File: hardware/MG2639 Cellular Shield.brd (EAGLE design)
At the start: 53.3 x 73.7 mm, 48 parts, among them J1 SIMHOLDER, Q1 MMBT2222A, U1 TXB0108, U2 SPX29302, U4 ARDUINO_R3_SHIELD, U5 MG2639V3

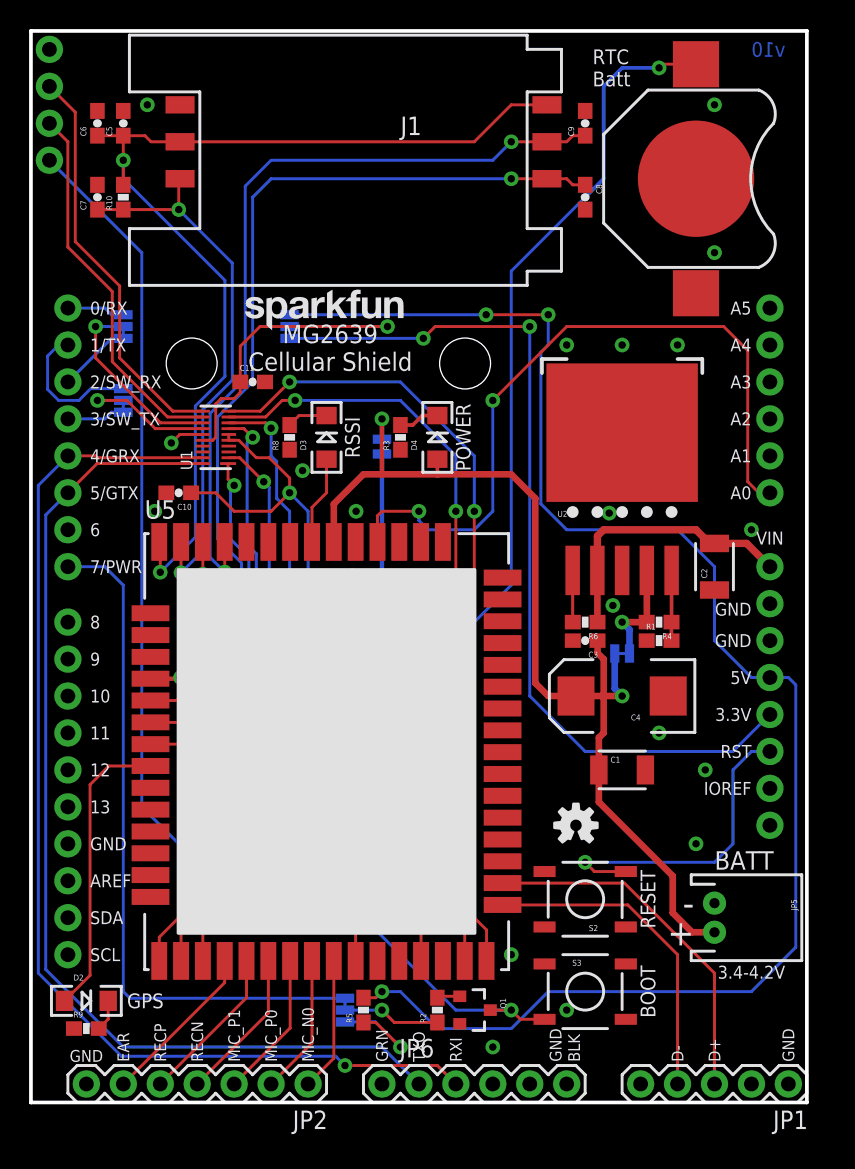
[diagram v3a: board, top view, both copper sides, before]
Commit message: re-routing around TXB0108, cleaning up some silk.
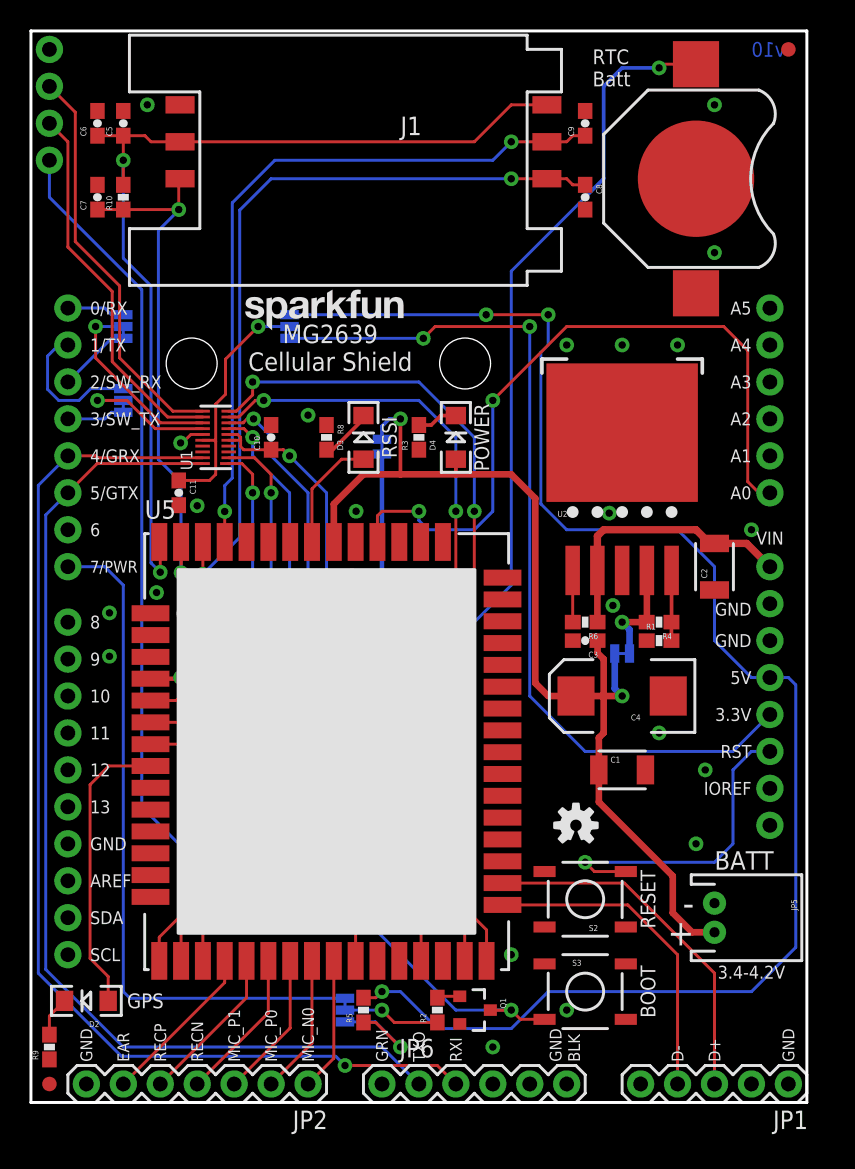
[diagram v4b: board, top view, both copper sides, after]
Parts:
- added FID1, FID2: FIDUCIAL1X2, SparkFun-Aesthetics:FIDUCIAL-1X2
- moved C11 9.16 mm to (10.2, 41.9), turned to 270 degrees
- moved C10 7.41 mm to (16.5, 45.7), turned to 90 degrees
- moved R9 2.84 mm to (1.27, 3.81), turned to 90 degrees
- moved D3 2.54 mm to (22.9, 45.7)
- moved R8 2.54 mm to (20.3, 45.7), turned to 270 degrees
- moved R3 1.27 mm to (26.7, 45.7)
- moved D4 1.27 mm to (29.2, 45.7)
- turned D2 to 180 degrees
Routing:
- net VCCB: track 25.9 -> 17.2 mm
- net SIM_RST: track 54.8 -> 49.7 mm
- net VDDIO: track 53.4 -> 48.5 mm
- net SIM_CLK: track 56.9 -> 53.1 mm
- net VSIM: track 70.7 -> 68.3 mm
- net N$7: track 6.10 -> 8.03 mm
- net SIM_DATA: track 37.9 -> 36.1 mm
- net RX-2.8V: track 41.1 -> 42.6 mm
- net TX2-2.8V: track 54.9 -> 56.1 mm
- net 3.8V: track 71.0 -> 71.9 mm
- net TX-2.8V: track 43.3 -> 44.2 mm
- net N$8: track 2.81 -> 3.65 mm
- net RX2-2.8V: track 52.6 -> 53.4 mm
- net GND: track 2.39 -> 1.75 mm, vias 22 -> 26
- net N$9: track 2.17 -> 2.76 mm
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
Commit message: adding 22 ohm resistors to D+/D-. placing more vias around vreg.
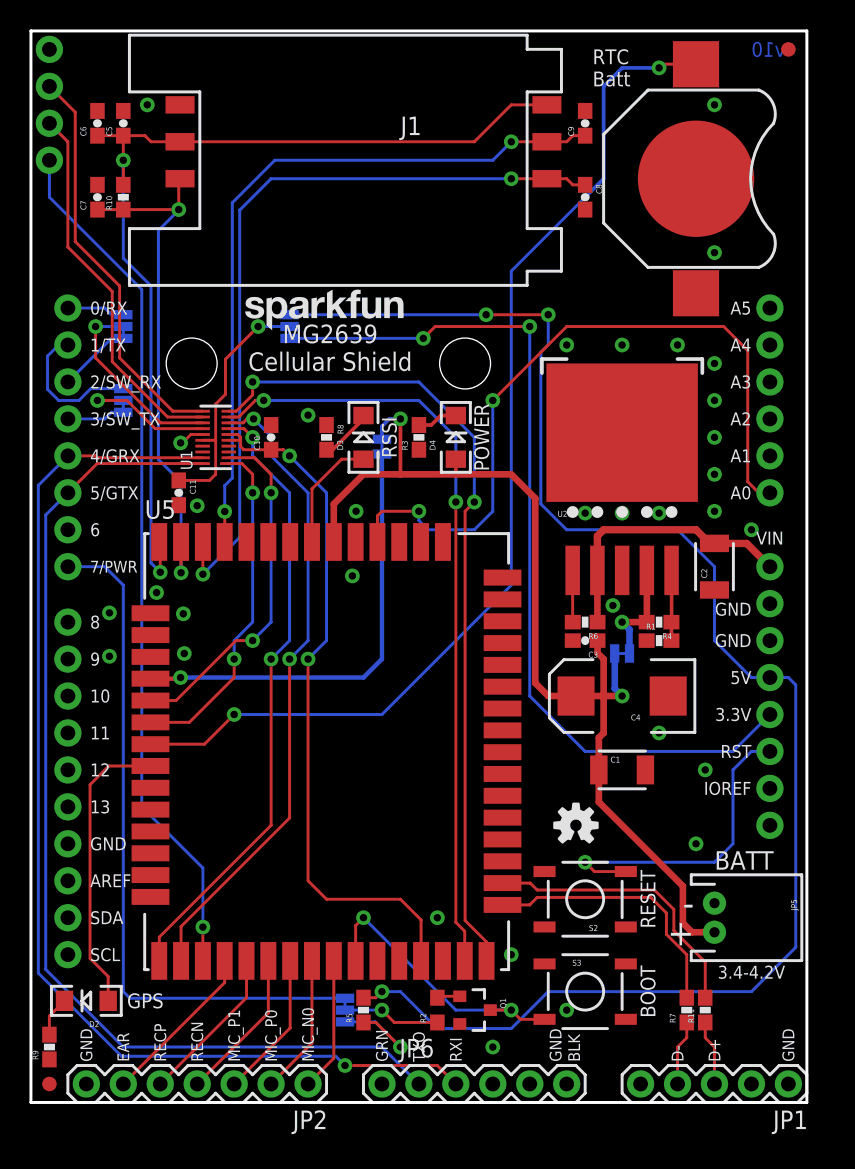
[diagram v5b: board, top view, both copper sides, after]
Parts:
- added R11, R7: 22, SparkFun-Resistors:0603-RES
- R2: device SparkFun-Resistors:0603-RES -> SparkFun-Resistors:0603
- moved FRAME1 28.1 mm to (-7.62, -22.9)
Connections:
- new net N$10: JP1.3, R11.1
- new net N$2: JP1.4, R7.1
- net USB+: now also R11.2; no longer JP1.3
- net USB-: now also R7.2; no longer JP1.4
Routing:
- net USB+: track 24.8 -> 19.5 mm
- net N$10: track 0.00 -> 4.49 mm
- net N$2: track 0.00 -> 4.49 mm
- net USB-: track 22.3 -> 18.3 mm
- net TX2-2.8V: track 56.1 -> 56.7 mm
- net GND: vias 26 -> 33

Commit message: rearranging LEDs - moving GPS LED up with others.
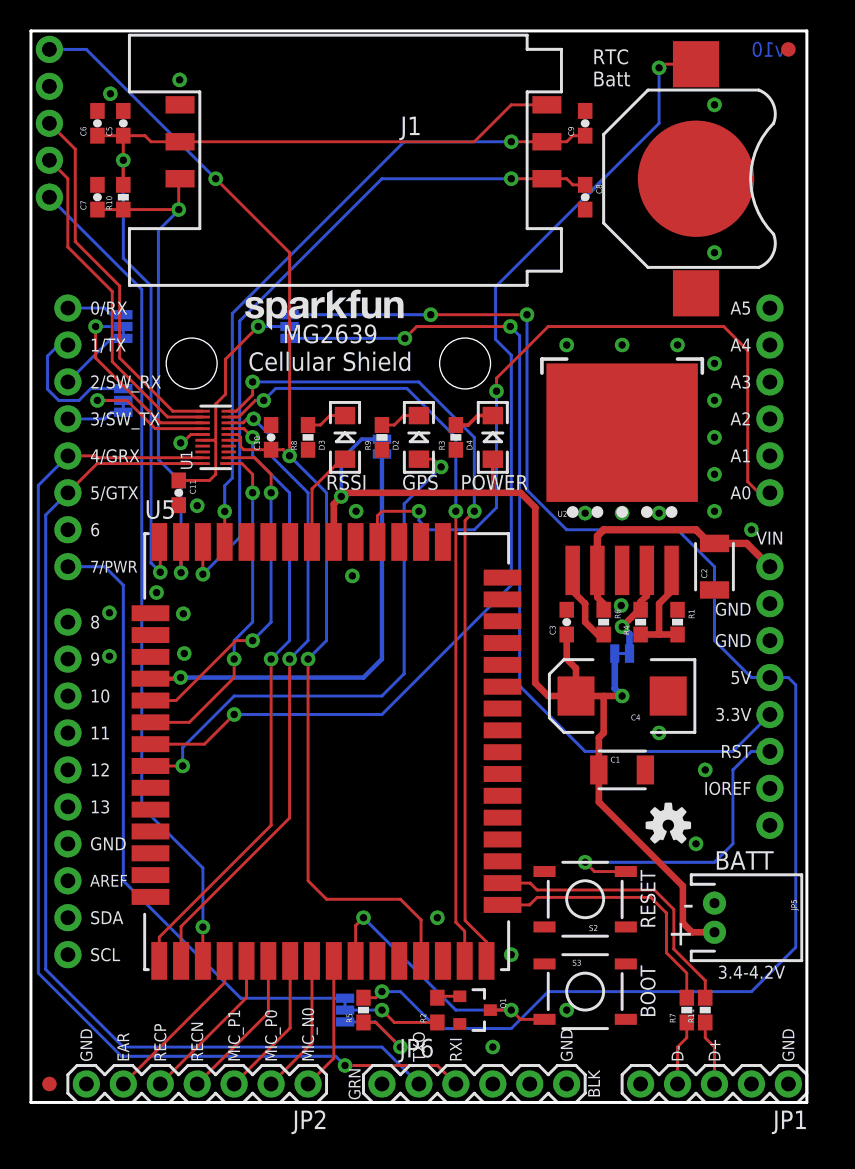
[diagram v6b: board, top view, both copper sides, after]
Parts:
- added JP7: M01PTH, SparkFun-Connectors:1X01
- moved R9 47.7 mm to (24.1, 45.7)
- moved D2 45.0 mm to (26.7, 45.7), turned to 90 degrees
- moved LOGO2 6.35 mm to (43.8, 19.1)
- moved JP4 2.54 mm to (1.27, 64.8)
- moved D4 2.54 mm to (31.8, 45.7)
- moved JP3 2.54 mm to (1.27, 62.2)
- moved R3 2.54 mm to (29.2, 45.7)
- moved C3 1.80 mm to (36.8, 33.0), turned to 90 degrees
- moved R1 1.80 mm to (44.5, 33.0), turned to 270 degrees
- moved R4 1.27 mm to (41.9, 33.0), turned to 90 degrees
- moved D3 1.27 mm to (21.6, 45.7)
- moved R8 1.27 mm to (19.1, 45.7), turned to 90 degrees
- moved R6 1.27 mm to (39.4, 33.0), turned to 270 degrees
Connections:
- new net ADCIN: U5.28
- new net GPIO0: U5.55
- new net GPIO1: U5.54
- new net GPIO2: U5.53
- net VDDIO: now also JP7.1
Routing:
- net VDDIO: track 48.5 -> 84.7 mm, vias 2 -> 3
- net GPS_FIX: track 20.1 -> 37.8 mm, vias 0 -> 2
- net ON/OFF: track 47.7 -> 43.2 mm
- net SIM_RST: track 49.7 -> 45.2 mm
- net SIM_CLK: track 53.1 -> 48.6 mm
- net RX2-HV: track 26.0 -> 23.4 mm
- net !SYSRST: track 59.4 -> 56.9 mm
- net TX2-HV: track 27.9 -> 25.3 mm
- net ADJUST: track 4.83 -> 7.30 mm
- net N$1: track 3.56 -> 5.53 mm
- net 5V: track 107.9 -> 106.7 mm
- net N$7: track 8.03 -> 6.76 mm
- net N$4: track 7.62 -> 6.69 mm
- net N$8: track 3.65 -> 2.81 mm
- net 3.3V: track 61.4 -> 60.6 mm
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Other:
- board text added: "2.8V"

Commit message: Switching TXB0108 to a TXB0104. Breaking out I2C pins, 2.8V. Fixing some silk.
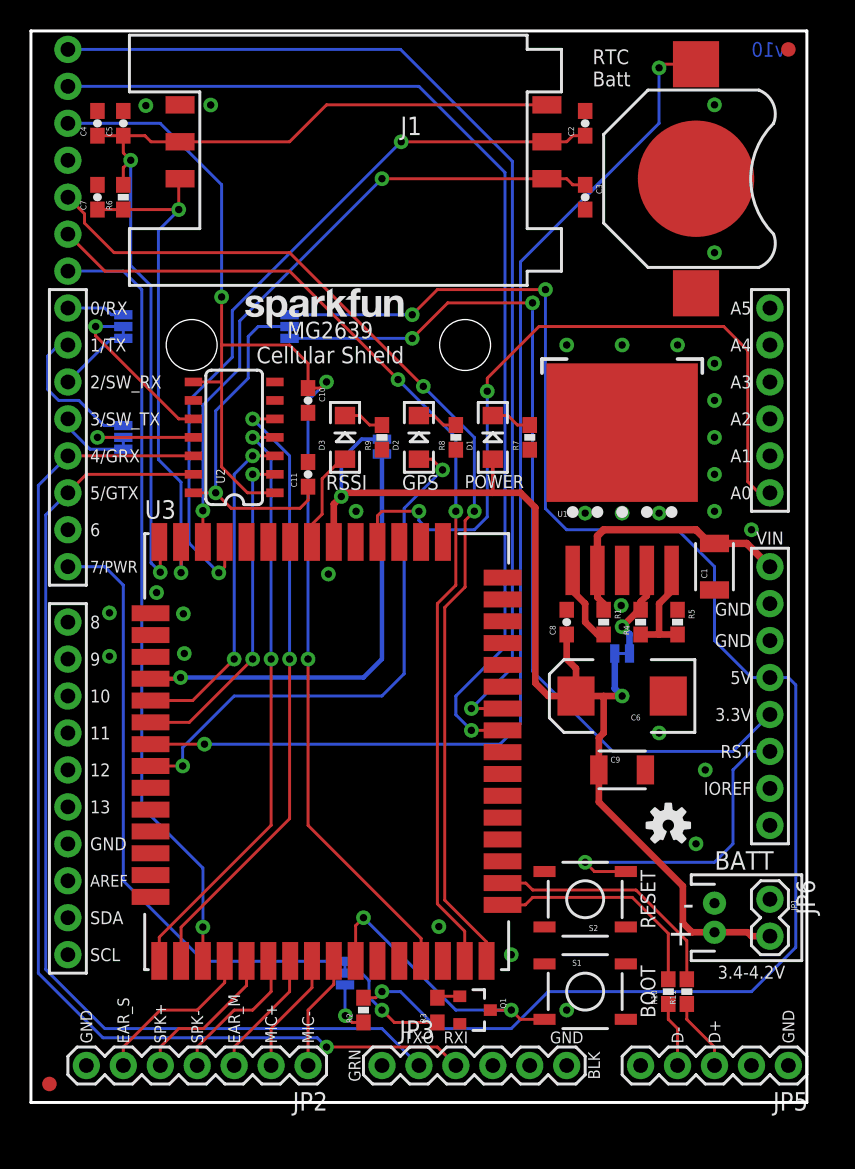
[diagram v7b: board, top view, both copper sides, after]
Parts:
- removed JP7: M01PTH, SparkFun-Connectors:1X01
- removed LOGO4: SFE_LOGO_NAME.1_INCH, SparkFun-Aesthetics:SFE_LOGO_NAME_.1
- added LOGO1: SFE_LOGO_NAME.1_INCH, SparkFun-Aesthetics:SFE_LOGO_NAME_.1
- C2: value 10uF -> 33pF; device SparkFun-Capacitors:1210 -> SparkFun-Capacitors:0603-CAP
- C3: value 0.1uF -> 33pF
- C4: value 100uF -> 1.0uF; device SparkFun-Capacitors:EIA7343 -> SparkFun-Capacitors:0603-CAP
- C6: value 1.0uF -> 100uF; device SparkFun-Capacitors:0603-CAP -> SparkFun-Capacitors:EIA7343
- C8: value 33pF -> 0.1uF
- C9: value 33pF -> 10uF; device SparkFun-Capacitors:0603-CAP -> SparkFun-Capacitors:1210
- JP1: value (none) -> LiPo; device SparkFun-Connectors:1X05 -> SparkFun-Connectors:JST-2-PTH
- JP3: value M01PTH -> FTDI_BASICPTH; device SparkFun-Connectors:1X01 -> SparkFun-Connectors:FTDI_BASIC
- JP4: device SparkFun-Connectors:1X03 -> SparkFun-Connectors:1X07
- JP5: value LiPo -> (none); device SparkFun-Connectors:JST-2-PTH -> SparkFun-Connectors:1X05
- JP6: value FTDI_BASICPTH -> M02PTH; device SparkFun-Connectors:FTDI_BASIC -> SparkFun-Connectors:1X02
- LOGO2: value OSHW-LOGOS -> SFE_LOGO_NAME_FLAME.2_INCH; device SparkFun-Aesthetics:OSHW-LOGO-S -> SparkFun-Aesthetics:SFE_LOGO_NAME_FLAME_.2
- LOGO3: value SFE_LOGO_NAME_FLAME.2_INCH -> OSHW-LOGOS; device SparkFun-Aesthetics:SFE_LOGO_NAME_FLAME_.2 -> SparkFun-Aesthetics:OSHW-LOGO-S
- R1: value 1K -> 10K
- R10: value 10K -> 22
- R2: value 4.7K -> 1K; device SparkFun-Resistors:0603 -> SparkFun-Resistors:0603-RES
- R3: value 1K -> 4.7K; device SparkFun-Resistors:0603-RES -> SparkFun-Resistors:0603
- R7: value 22 -> 1K
- SJ1, SJ6: device SparkFun-Passives:PAD-JUMPER-2-NC_BY_TRACE_YES_SILK -> SparkFun-Passives:PAD-JUMPER-3-2OF3_NC_BY_TRACE_YES_SILK_FULL_BOX
- SJ2, SJ3: device SparkFun-Passives:PAD-JUMPER-3-2OF3_NC_BY_TRACE_YES_SILK_FULL_BOX -> SparkFun-Passives:PAD-JUMPER-2-NC_BY_TRACE_YES_SILK
- U1: value TXB0108 -> SPX29302; device Testing:UFDFN-20 -> SparkFun-PowerIC:Q5-DD_SPX29300
- U2: value SPX29302 -> (none); device SparkFun-PowerIC:Q5-DD_SPX29300 -> SparkFun-DigitalIC:SO14
- moved R10 66.2 mm to (43.8, 7.62)
- moved JP3 63.9 mm to (24.1, 2.54), flipped to the top, turned to 0 degrees
- moved C4 53.4 mm to (4.57, 67.3), turned to 90 degrees
- moved C6 53.4 mm to (40.6, 27.9), turned to 180 degrees
- moved C9 44.5 mm to (40.6, 22.9), turned to 0 degrees
- moved R6 44.1 mm to (6.35, 62.2), turned to 90 degrees
- moved SJ6 41.0 mm to (6.35, 53.3), turned to 270 degrees
- moved R7 40.8 mm to (34.3, 45.7)
- moved R3 39.4 mm to (27.9, 6.35)
- moved SJ1 36.3 mm to (21.6, 8.89), turned to 90 degrees
- moved R5 34.3 mm to (44.5, 33.0), turned to 270 degrees
- moved C2 31.8 mm to (38.1, 67.3)
- moved SJ2 31.0 mm to (40.6, 30.9), turned to 0 degrees
- moved JP6 29.5 mm to (50.8, 14.0), turned to 270 degrees
- moved C3 29.2 mm to (38.1, 62.2), turned to 270 degrees
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- renumbered D4 to D1, S3 to S1, U4 to J2, U5 to U3
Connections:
- removed net GPIO0: U3.55
- removed net GPIO1: U3.54
- removed net GPIO2: U3.53
- removed net HJ: U1.3
- removed net JK: U1.4
- removed net KK: U1.18
- removed net LL: U1.17
- removed net RX2-HV: JP4.1, U1.12
- removed net TX2-HV: JP4.2, U1.11
- new net GPIO1/SCL: JP4.1, U3.54
- new net GPIO2/SDA: JP4.2, U3.53
- net !SYSRST: now also JP4.7; no longer JP3.1
- net 3.3V: now also SJ4.3; no longer SJ5.3
- net 3.8V: now also C6.A, C8.1, C9.1, JP1.2, JP6.2, SJ2.2, SJ3.1; no longer C1.1, C3.1, C4.A, JP5.2, SJ1.1, SJ6.2
- net 5V: now also R2.2, SJ4.1; no longer R5.2, SJ5.1
- net ADJUST: now also R5.2, U1.5; no longer R1.2, U2.5
- net GND: now also C1.1, C2.2, C4.2, C6.C, JP3.GND, JP4.4, JP6.1, R5.1, R7.1, U1.3, U1.6, U2.7; no longer C1.2, C2.1, C4.C, C6.2, JP4.3, JP6.GND, R1.1, R3.1, U1.15, U2.3, U2.6
- net GRX-2.8V: now also U2.3; no longer U1.2
- net GRX-HV: now also JP3.TXO, U2.12; no longer JP6.TXO, U1.19
- net GTX-2.8V: now also U2.2; no longer U1.1
- net GTX-HV: now also JP3.RXI, U2.13; no longer JP6.RXI, U1.20
- net N$1: now also R1.2, U1.1; no longer R6.2, U2.1
- net N$10: now also JP5.3; no longer JP1.3
- net N$17: now also R7.2; no longer R3.2
- net N$2: now also JP5.4, R10.1; no longer JP1.4, R7.1
- net N$3: now also R3.2; no longer R2.2
- net N$4: now also SJ2.1, U1.4; no longer SJ6.1, U2.4
- net N$5: now also R3.1, SJ1.2; no longer R2.1, SJ2.2
- net N$6: now also R2.1, SJ1.1; no longer R5.1, SJ2.1
- net N$8: now also R9.2; no longer R8.2
- net N$9: now also R8.2; no longer R9.2
- net ON/OFF: now also SJ1.3; no longer SJ2.3
- net RX-2.8V: now also U2.4; no longer U1.7
- net RX-HV: now also SJ5.2, U2.11; no longer SJ3.2, U1.14
- net RX-SOFT: now also SJ6.3; no longer SJ4.3
- net RX2-2.8V: now also JP4.6; no longer U1.9
- net RXI: now also SJ6.1; no longer SJ4.1
- net SIM_CLK: now also C3.1; no longer C8.1
- net SIM_DATA: now also R6.1; no longer R10.1
- net SIM_RST: now also C2.1; no longer C9.1
- net TX-2.8V: now also U2.5; no longer U1.8
- net TX-HV: now also SJ6.2, U2.10; no longer SJ4.2, U1.13
- net TX-SOFT: now also SJ5.3; no longer SJ3.3
- net TX2-2.8V: now also JP4.5; no longer U1.10
- net TXO: now also SJ5.1; no longer SJ3.1
- net USB-: now also R10.2; no longer R7.2
- net VCCB: now also SJ4.2, U2.14; no longer SJ5.2, U1.16
- net VDDIO: now also JP4.3, U2.1, U2.8; no longer JP7.1, U1.5, U1.6
- net VRAW: now also C1.2, R1.1, U1.2; no longer C2.2, R6.1, U2.2
- net VSIM: now also C4.1, R6.2; no longer C6.1, R10.2
- net V_GPS: now also SJ3.2; no longer SJ1.2
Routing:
- net GPIO2/SDA: track 0.00 -> 74.8 mm, vias 0 -> 1
- net GPIO1/SCL: track 0.00 -> 74.7 mm, vias 0 -> 1
- net TX2-HV: track 25.3 -> 0.00 mm
- net RX2-HV: track 23.4 -> 0.00 mm
- net TX2-2.8V: track 56.7 -> 73.2 mm
- net RX2-2.8V: track 54.1 -> 69.8 mm
- net VCCB: track 17.2 -> 24.3 mm
- net VDDIO: track 84.7 -> 91.2 mm
- net SIM_RST: track 45.2 -> 51.6 mm
- net GPS_RTC: track 72.6 -> 77.7 mm
- net N$6: track 8.36 -> 3.56 mm
- net SIM_CLK: track 48.6 -> 44.2 mm
- net 3.8V: track 72.0 -> 76.0 mm
- net !SYSRST: track 56.9 -> 53.5 mm
- net 5V: track 106.7 -> 109.9 mm
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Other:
- board text added: "EAR_M"
- board text added: "EAR_S"
- board text added: "GPIO/2SDA"
- board text added: "GPIO1/SCL"
- board text added: "MIC+"
- board text added: "MIC-"
- board text added: "SPK+"
- board text added: "SPK-"
- board text removed: "EAR"
- board text removed: "MIC_N0"
- board text removed: "MIC_P0"
- board text removed: "MIC_P1"
- board text removed: "RECN"
- board text removed: "RECP"

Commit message: Routing UART1 to FTDI header instead of GPS. Adding TP's. Fixing silk. Routing out GPS battery pull-out area.
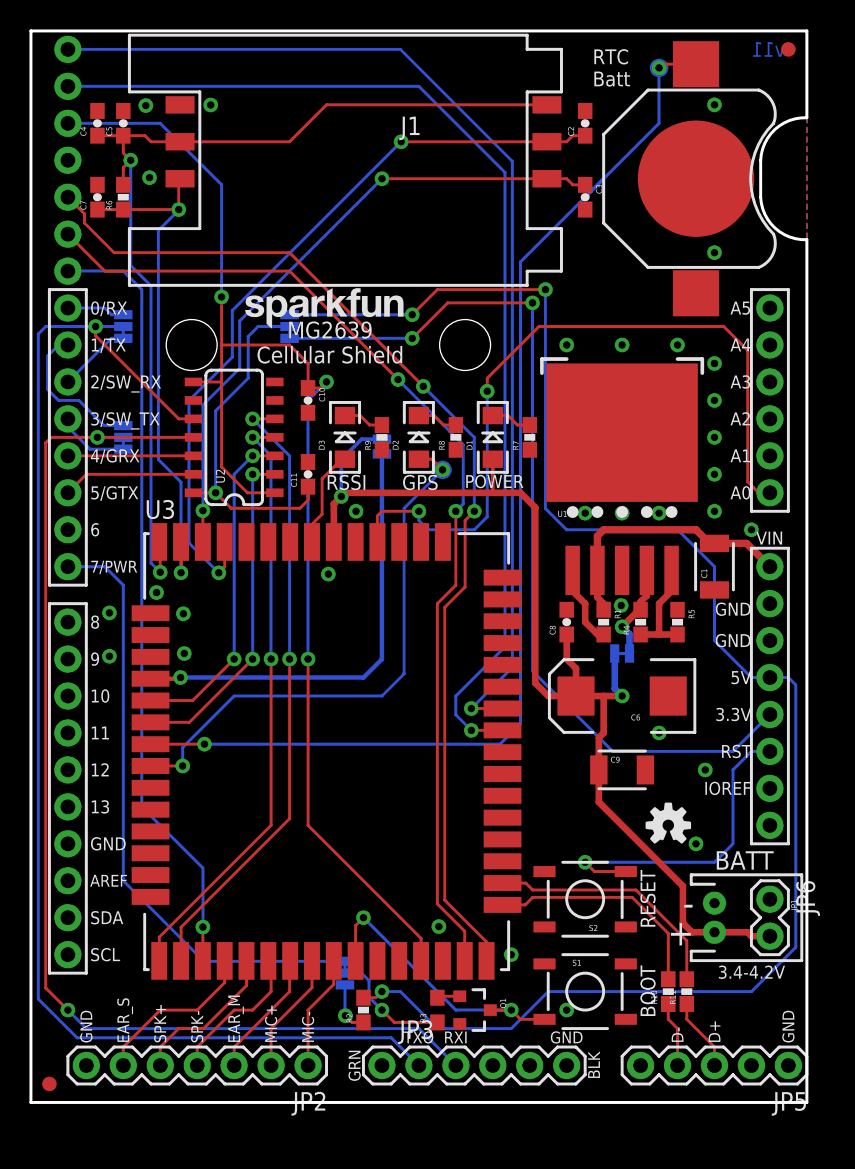
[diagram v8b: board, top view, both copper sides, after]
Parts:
- added TP1, TP2: (no value), SparkFun-Passives:PAD.03X.05
- SJ1: device SparkFun-Passives:PAD-JUMPER-3-2OF3_NC_BY_TRACE_YES_SILK_FULL_BOX -> SparkFun-Passives:PAD-JUMPER-2-NC_BY_TRACE_YES_SILK
- SJ3: device SparkFun-Passives:PAD-JUMPER-2-NC_BY_TRACE_YES_SILK -> SparkFun-Passives:PAD-JUMPER-3-2OF3_NC_BY_TRACE_YES_SILK_FULL_BOX
- moved SJ1 36.3 mm to (24.1, 45.1), turned to 270 degrees
- moved SJ3 36.3 mm to (21.6, 8.89), turned to 90 degrees
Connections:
- net 3.8V: now also SJ1.1; no longer SJ3.1
- net GPS_FIX: now also TP1.P$1
- net GPS_RTC: now also TP2.P$1
- net GRX-HV: no longer JP3.TXO
- net GTX-HV: no longer JP3.RXI
- net N$5: now also SJ3.2; no longer SJ1.2
- net N$6: now also SJ3.1; no longer SJ1.1
- net ON/OFF: now also SJ3.3; no longer SJ1.3
- net RX-HV: now also JP3.TXO
- net TX-HV: now also JP3.RXI
- net V_GPS: now also SJ1.2; no longer SJ3.2
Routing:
- net TX-HV: track 11.6 -> 89.6 mm
- net RX-HV: track 8.38 -> 80.0 mm, vias 1 -> 2
- net GRX-HV: track 76.4 -> 8.63 mm, vias 1 -> 0
- net GTX-HV: track 70.9 -> 9.16 mm
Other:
- outline, holes or cut-outs redrawn
- board text added: "v11"
- board text removed: "v10"
